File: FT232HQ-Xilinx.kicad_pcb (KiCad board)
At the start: 2 copper layers, 39.7 x 20.3 mm, 33 parts, among them J1 USB_C_Receptacle_USB2.0_16P, J2 Conn_02x07_Odd_Even, J3 Conn_02x05_Odd_Even, U1 TLV9061xDBV, U2 TLV75533PDBV, U3 SN74AVC4T774PW, U4 12M, U5 FT232H, U6 93LCxxBxxOT

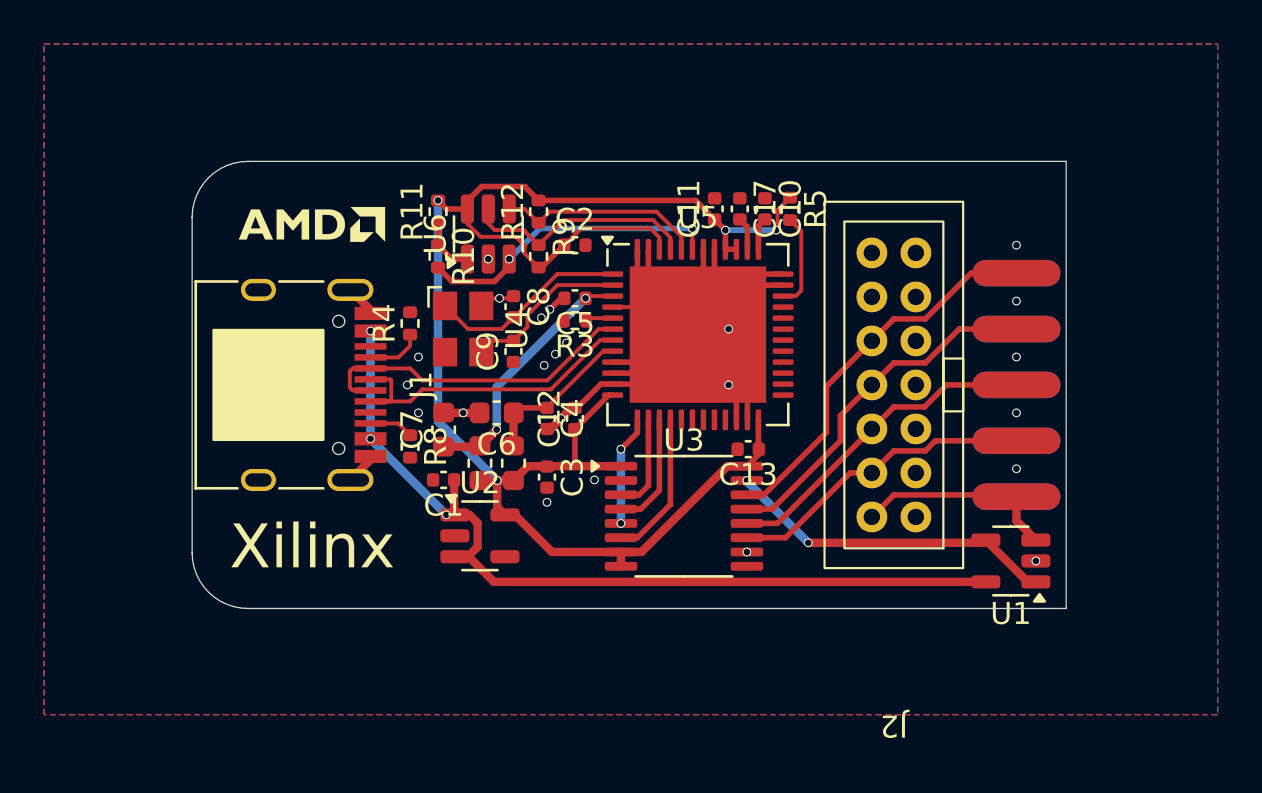
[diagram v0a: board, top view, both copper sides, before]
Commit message: fix: 1. Add 10k between vref and gnd. 2. Remove vias on pads.
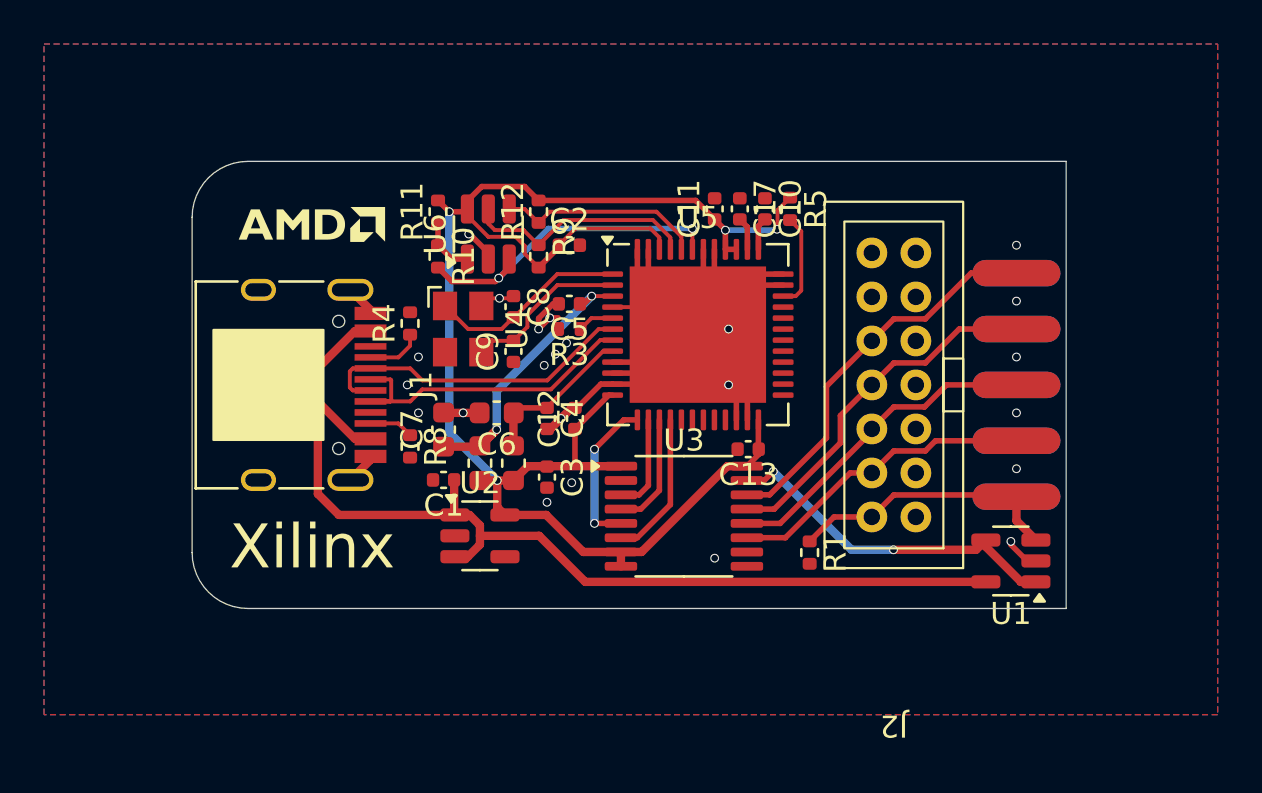
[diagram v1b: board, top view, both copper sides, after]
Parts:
- added R1: 10k, Resistor_SMD:R_0402_1005Metric, F.Cu at (147.4, 83.6)
- moved R3 0.46 mm to (136.5, 73.5)
- moved C5 0.36 mm to (136.5, 72.3)
- moved C2 0.25 mm to (136.5, 69.7)
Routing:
- net GND: track 63.6 -> 39.5 mm
- net +5V: track 39.3 -> 48.2 mm, vias 3 -> 0
- net VREF: track 9.36 -> 12.5 mm
- net /TCK: track 5.01 -> 7.08 mm
- net VREF_F: track 14.8 -> 16.6 mm
- net +3V3: track 73.4 -> 72.0 mm
- net /EEDIO: track 13.6 -> 14.4 mm
- net /VPHY: track 12.6 -> 13.3 mm
- net Net-(U5-REF): track 1.09 -> 1.66 mm

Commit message: fix: c13 drc error
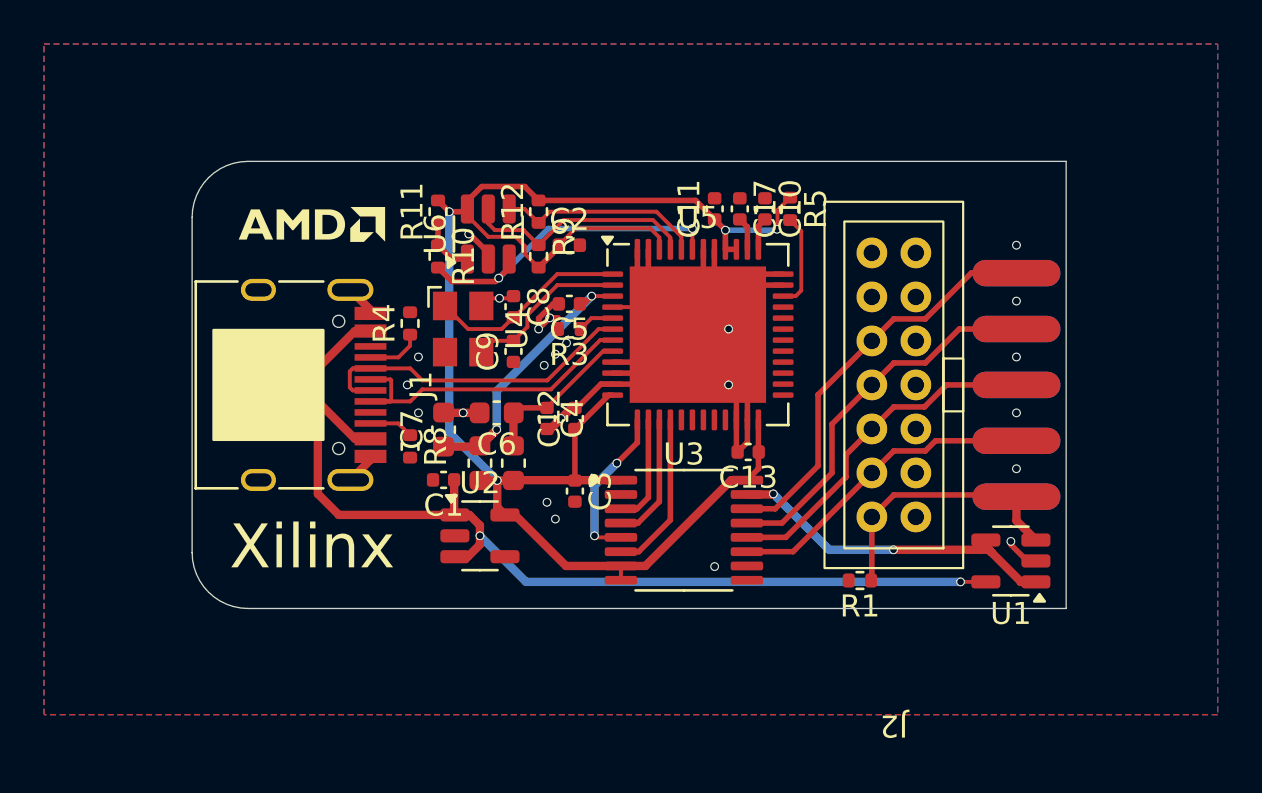
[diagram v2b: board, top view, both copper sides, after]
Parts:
- moved R1 2.62 mm to (149.7, 84.9), turned to 180 degrees
- moved C3 1.42 mm to (136.7, 80.8)
- moved U3 0.63 mm to (141.7, 82.6)
- moved C13 0.13 mm to (144.6, 79.1)
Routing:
- net GND: track 39.5 -> 42.5 mm
- net +3V3: track 72.0 -> 73.4 mm
- net /TMS: track 6.09 -> 7.39 mm
- net /TCKR: track 14.8 -> 15.7 mm
- net /TMSR: track 13.4 -> 14.3 mm
- net /TDOR: track 14.5 -> 15.4 mm
- net /TDIR: track 16.5 -> 17.3 mm
- net /TDI: track 4.41 -> 4.99 mm
- net +5V: vias 0 -> 2

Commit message: update
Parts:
- removed J2: Conn_02x07_Odd_Even, 1st_commonly:Molex_Xilinx_02x07_P2.0mm_Vertical
- added C14: 104, Capacitor_SMD:C_0402_1005Metric, F.Cu at (148.5, 84.4)
- moved U1 5.34 mm to (151.2, 83.9)
- moved J3 4.57 mm to (152.2, 76.0)
- moved R1 3.87 mm to (153.2, 83.4), turned to -90 degrees
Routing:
- net VREF: track 12.1 -> 1.72 mm
- net VREF_F: track 16.8 -> 9.02 mm
- net +5V: track 48.2 -> 43.3 mm
- net /TMSR: track 14.3 -> 10.3 mm
- net /TCKR: track 15.7 -> 12.0 mm
- net /TDIR: track 17.3 -> 15.5 mm
- net /TDOR: track 15.4 -> 14.1 mm
- net /TCK: track 7.31 -> 6.04 mm
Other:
- board size 39.7 x 20.3 mm -> 34.9 x 20.3 mm

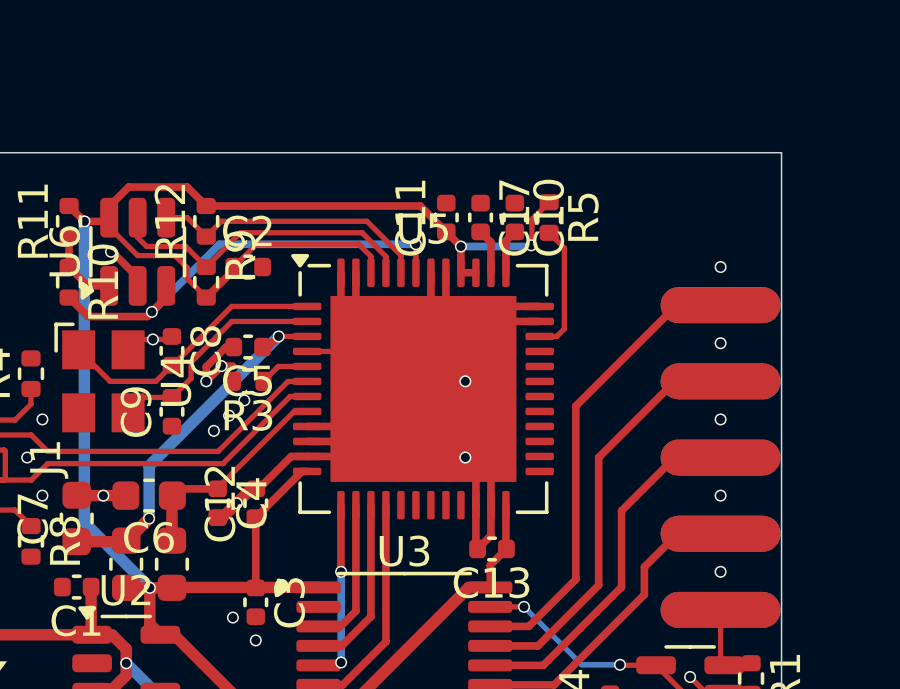
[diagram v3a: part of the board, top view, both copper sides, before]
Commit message: set ac9 as SLEEP# LED
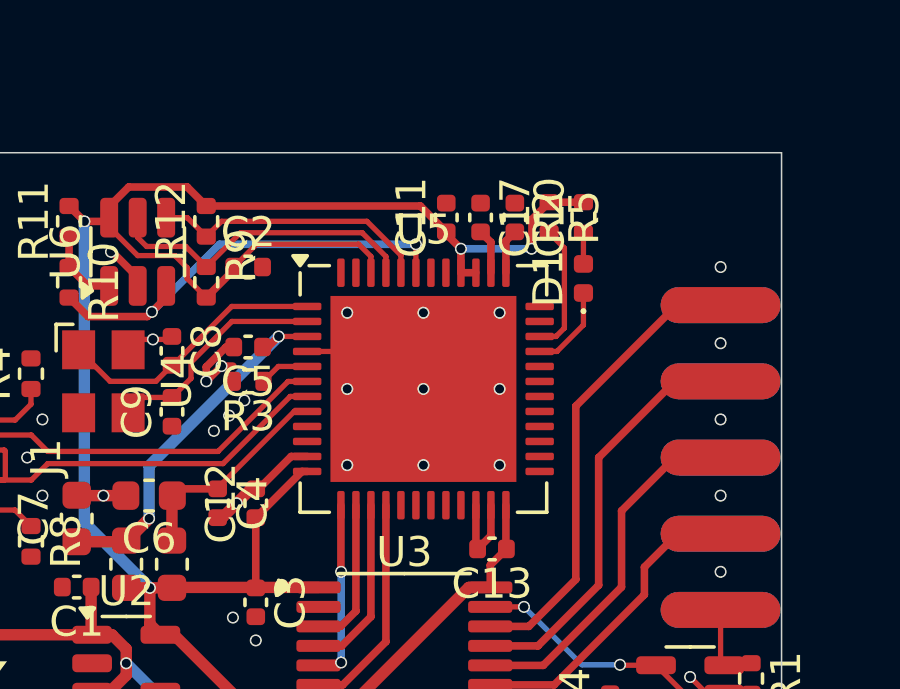
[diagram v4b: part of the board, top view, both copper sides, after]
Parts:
- added D1: LED, LED_SMD:LED_0402_1005Metric, F.Cu at (147.6, 70.0)
- added R2: 10k, Resistor_SMD:R_0402_1005Metric, F.Cu at (147.6, 68.0)
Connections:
- U5 pad 33: unconnected-(U5-ACBUS9-Pad33) -> Net-(D1-K)
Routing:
- net GND: track 42.7 -> 20.3 mm, vias 23 -> 30
- net Net-(D1-K): track 0.00 -> 2.89 mm
- net +3V3: track 73.4 -> 74.6 mm
- net Net-(D1-A): track 0.00 -> 1.04 mm

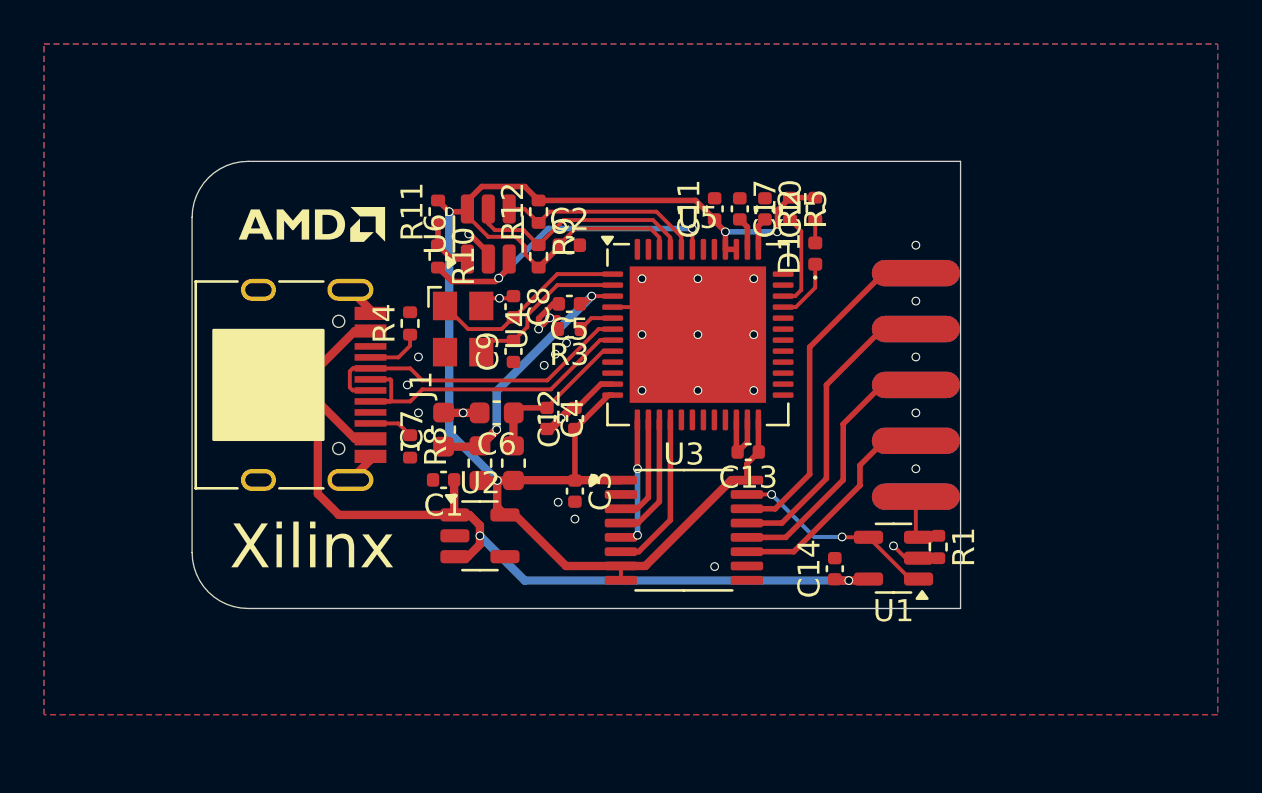
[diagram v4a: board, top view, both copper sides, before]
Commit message: remove ldo and useless resistance
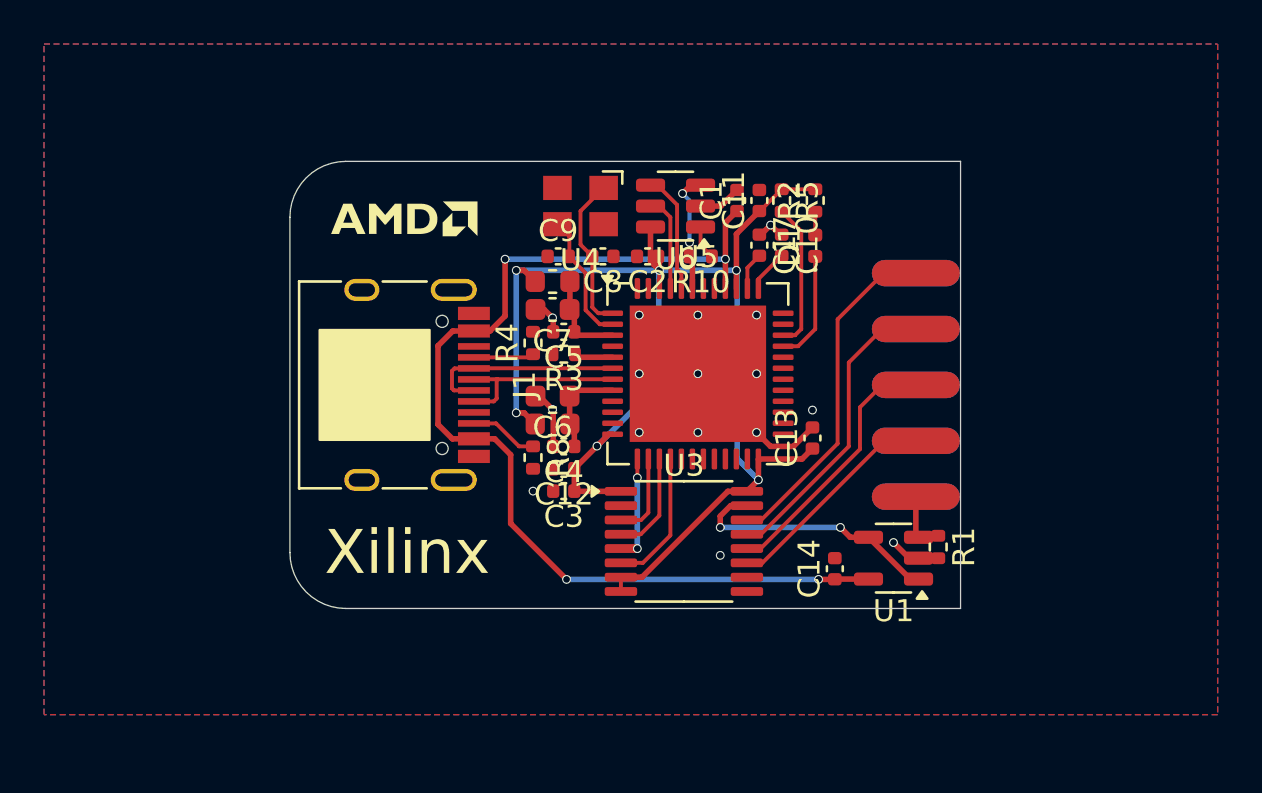
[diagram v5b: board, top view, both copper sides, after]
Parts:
- removed R11, R12, R9: 10k, Resistor_SMD:R_0402_1005Metric
- removed U2: TLV75533PDBV, Package_TO_SOT_SMD:SOT-23-5
- moved C1 18.4 mm to (144.1, 67.6), turned to 90 degrees
- moved R10 11.9 mm to (142.4, 70.2), turned to 180 degrees
- moved L2 8.89 mm to (135.7, 71.3), turned to 0 degrees
- moved U6 8.60 mm to (141.3, 67.9), turned to 180 degrees
- moved U4 7.73 mm to (137.0, 67.9), turned to 180 degrees
- moved C7 7.37 mm to (135.7, 72.6), turned to 180 degrees
- moved R4 5.66 mm to (134.8, 74.1)
- moved R8 5.61 mm to (134.8, 79.3)
- moved C9 4.77 mm to (135.9, 70.2), turned to 0 degrees
- moved J1 4.70 mm to (128.1, 76.0)
- moved C8 4.66 mm to (138.0, 70.2), turned to 180 degrees
- moved C2 3.59 mm to (140.0, 70.2), turned to 180 degrees
- moved C13 2.99 mm to (147.5, 78.4), turned to 90 degrees
- moved C6 2.65 mm to (135.7, 76.5)
- moved L1 2.51 mm to (135.7, 77.8), turned to 0 degrees
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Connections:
- U5 pad 40: +3V3 -> +5V
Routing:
- net /EEDIO: track 14.4 -> 4.85 mm
- net /VPHY: track 13.3 -> 3.87 mm, vias 2 -> 0
- net GND: track 20.3 -> 11.5 mm, vias 30 -> 16
- net +3V3: track 74.6 -> 66.6 mm, vias 4 -> 6
- net /DP: track 15.0 -> 8.26 mm
- net /EECS: track 10.7 -> 3.96 mm
- net /DN: track 14.9 -> 9.17 mm
- net +5V: track 43.3 -> 47.8 mm, vias 2 -> 4
- net /EECLK: track 9.35 -> 5.15 mm
- net /VPLL: track 6.81 -> 3.76 mm
- net VREF_F: track 9.02 -> 11.5 mm
- net Net-(U5-~{RESET}): track 4.33 -> 6.64 mm
- net Net-(D1-K): track 2.89 -> 5.08 mm
- net /OSCI: track 9.05 -> 7.12 mm
- net /OSCO: track 7.54 -> 5.91 mm
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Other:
- board size 34.9 x 20.3 mm -> 30.5 x 20.3 mm

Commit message: little fix
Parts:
- moved U1 1.91 mm to (149.3, 83.9)
- moved C14 1.78 mm to (146.7, 84.4)
- moved R1 1.40 mm to (151.8, 83.4)
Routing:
- net GND: track 11.5 -> 14.4 mm, vias 16 -> 21
- net +5V: track 47.8 -> 45.9 mm
- net VREF: track 1.72 -> 3.27 mm
- net VREF_F: track 11.5 -> 10.8 mm

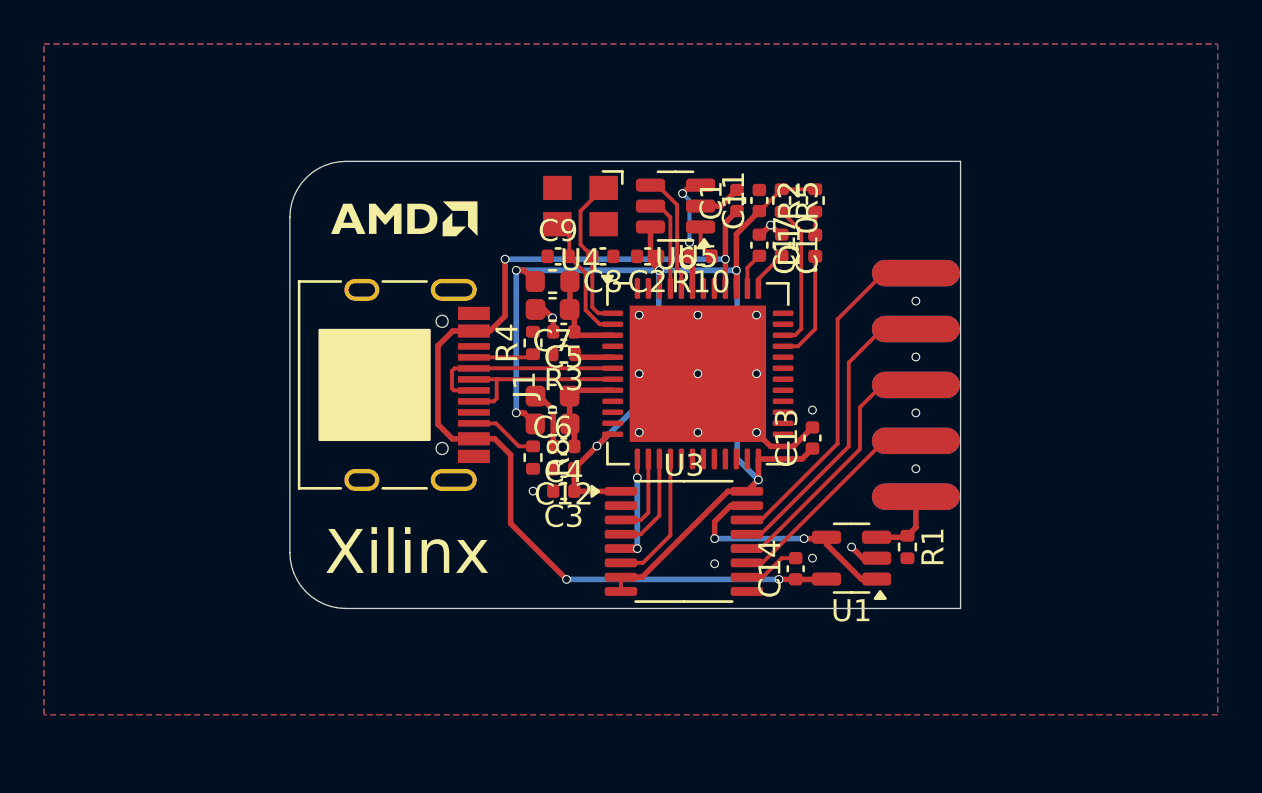
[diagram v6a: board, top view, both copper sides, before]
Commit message: add raspberry jst-sh1.0 uart
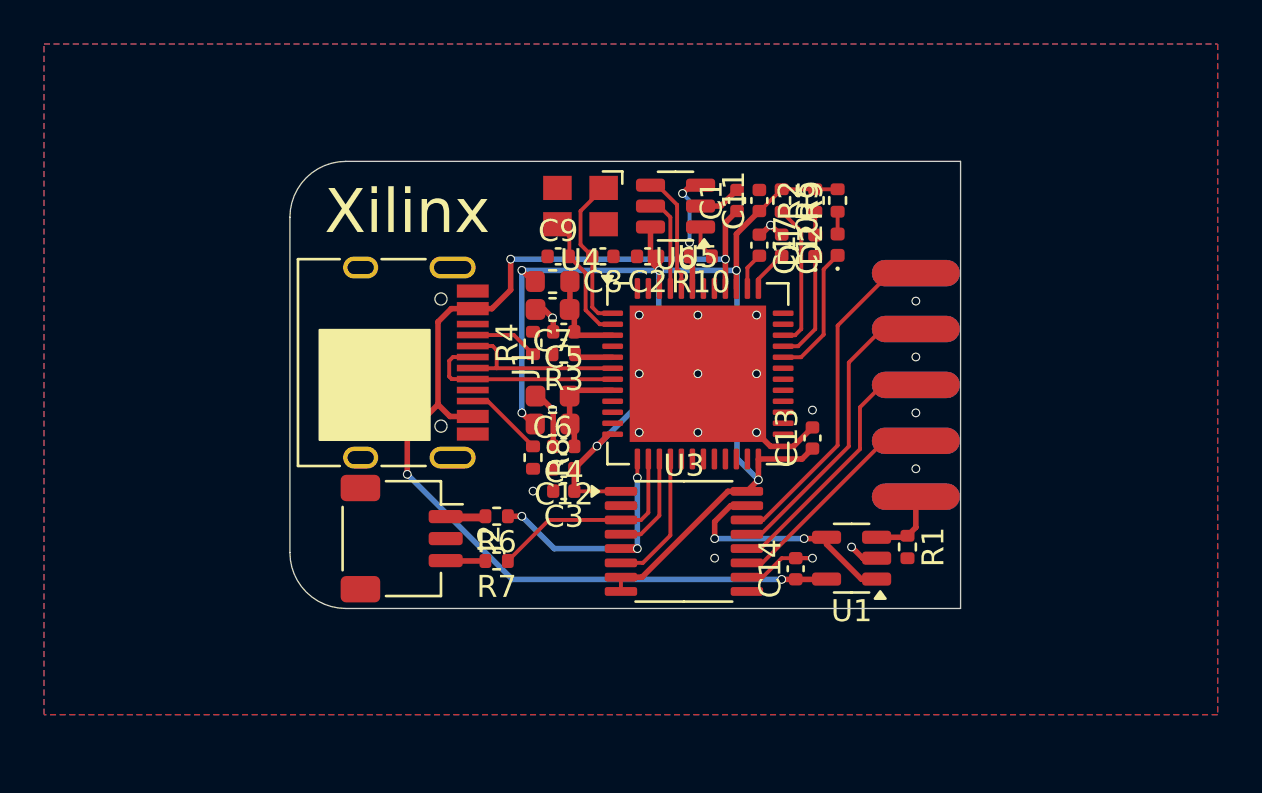
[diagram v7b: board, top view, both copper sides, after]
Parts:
- added D2: LED, LED_SMD:LED_0402_1005Metric, F.Cu at (148.6, 69.6)
- added J2: Conn_01x03_MountingPin, Connector_JST:JST_SH_SM03B-SRSS-TB_1x03-1MP_P1.00mm_Horizontal, F.Cu at (128.8, 83.0)
- added R6: 100, Resistor_SMD:R_0402_1005Metric, F.Cu at (133.2, 82.0)
- added R7: 100, Resistor_SMD:R_0402_1005Metric, F.Cu at (133.2, 84.0)
- added R9: 10k, Resistor_SMD:R_0402_1005Metric, F.Cu at (148.6, 67.6)
- moved J1 1.02 mm to (128.0, 75.0)
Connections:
- net Net-(D1-K) renamed /AC9
- U5 pad 32: unconnected-(U5-ACBUS8-Pad32) -> /AC8
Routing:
- net /TCK: track 4.82 -> 11.3 mm, vias 2 -> 3
- net /AC8: track 0.00 -> 6.13 mm
- net /TDI: track 3.82 -> 9.73 mm
- net Net-(J2-Pin_1): track 0.00 -> 3.61 mm
- net +5V: track 45.9 -> 49.1 mm
- net Net-(J2-Pin_3): track 0.00 -> 1.79 mm
- net GND: track 14.4 -> 15.9 mm
- net /DP: track 8.26 -> 9.33 mm
- net Net-(D2-A): track 0.00 -> 1.01 mm
- net /DN: track 9.17 -> 8.34 mm
- net /CC1: track 2.54 -> 3.10 mm
